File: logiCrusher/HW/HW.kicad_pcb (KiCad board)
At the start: 2 copper layers, 33 x 90 mm, 49 parts, among them J1 Left, J3 Conn_02x05_Odd_Even, J4 Right, U1 LM2904DR, U2 LM2904DR, U3 R-783.3-0.5, U4 STM32F373CCTx, U5 LM2904DR, U6 LM2904DR

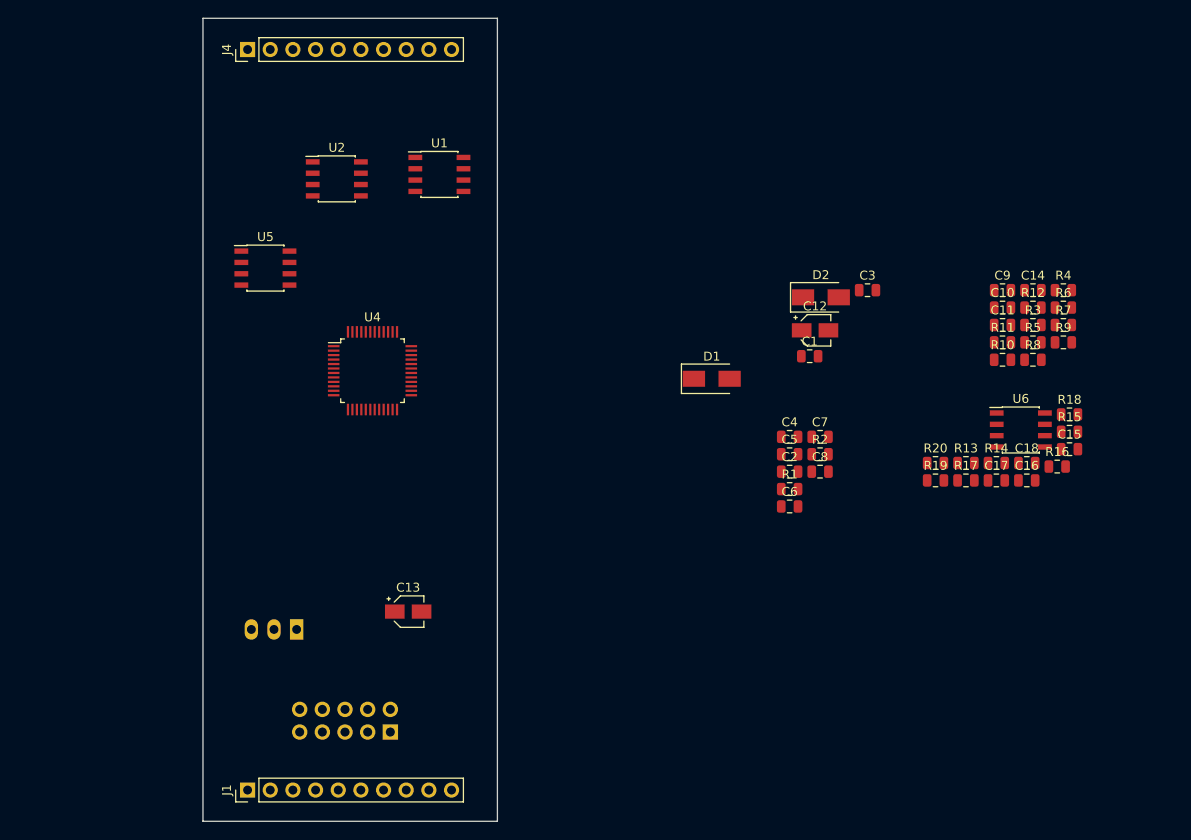
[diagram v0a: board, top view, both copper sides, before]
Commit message: Worked on the layout for the logicrusher
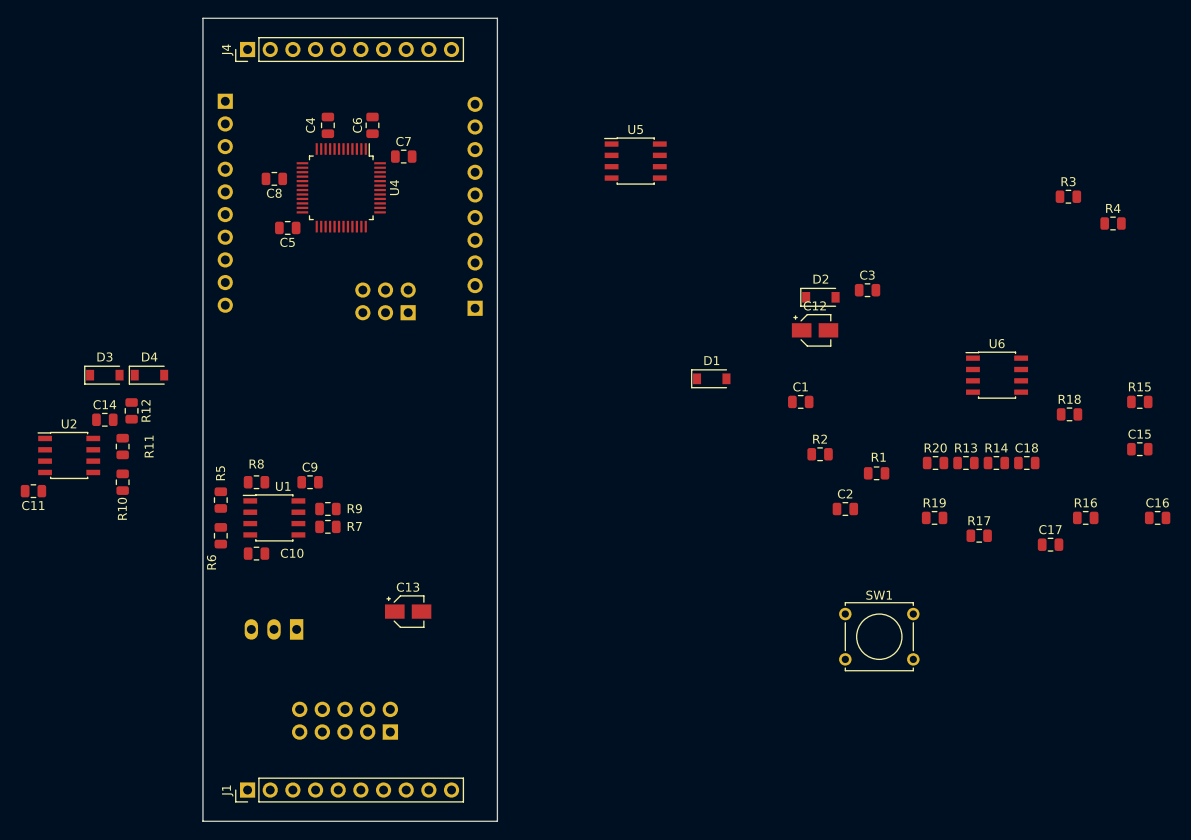
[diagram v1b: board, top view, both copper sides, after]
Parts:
- added D3: 1N5819HW-7-F, Diode_SMD:D_SOD-123, F.Cu at (99.0, 100.0)
- added D4: 1N5819HW-7-F, Diode_SMD:D_SOD-123, F.Cu at (104.0, 100.0)
- added J2: Conn_02x03_Odd_Even, Connector_PinHeader_2.54mm:PinHeader_2x03_P2.54mm_Vertical, B.Cu at (133.0, 93.0)
- added J5: Conn_01x10, Connector_PinHeader_2.54mm:PinHeader_1x10_P2.54mm_Vertical, B.Cu at (140.5, 92.5)
- added J6: Conn_01x10, Connector_PinHeader_2.54mm:PinHeader_1x10_P2.54mm_Vertical, B.Cu at (112.5, 69.3)
- added SW1: SW_Push, Button_Switch_THT:SW_Tactile_Straight_KSL0Axx1LFTR, F.Cu at (182.0, 126.8)
- D1, D2: value STTH102A -> 1N5819HW-7-F; footprint Diode_SMD:D_SMA -> Diode_SMD:D_SOD-123
- moved C11 110.2 mm to (91.0, 113.0), turned to 180 degrees
- moved C14 105.0 mm to (99.0, 105.0)
- moved R12 101.7 mm to (102.0, 104.0), turned to 270 degrees
- moved R10 99.6 mm to (101.0, 112.0), turned to 270 degrees
- moved R11 99.3 mm to (101.0, 108.0), turned to 270 degrees
- moved R6 97.8 mm to (112.0, 118.0), turned to 90 degrees
- moved R5 92.7 mm to (112.0, 114.0), turned to 270 degrees
- moved R8 88.1 mm to (116.0, 112.0), turned to 180 degrees
- moved C10 88.0 mm to (116.0, 120.0)
- moved R7 85.5 mm to (124.0, 117.0)
- moved R9 84.5 mm to (124.0, 115.0)
- moved C9 80.5 mm to (122.0, 112.0)
- moved C8 69.4 mm to (118.0, 78.0), turned to 180 degrees
- moved C6 63.3 mm to (129.0, 72.0), turned to 90 degrees
- moved C4 62.4 mm to (124.0, 72.0), turned to 90 degrees
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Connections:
- R20 pad 2: /OUT_Cond/Vout -> /AOUT0
- R5 pad 1: /IN_Cond/Vin -> /AIN0
- U4 pad 10: /MCU/ADC0 -> /POT3
- U4 pad 11: /MCU/ADC1 -> /POT2
- U4 pad 12: /MCU/ADC2 -> /POT1
- U4 pad 13: /MCU/ADC3 -> /POT0
- U4 pad 14: /MCU/Vout -> /OUT_Cond/Vin

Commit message: Spend a lot of time working on the logicCrusher HW
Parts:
- SW1: moved to B.Cu
- moved R4 102.7 mm to (111.5, 104.0), turned to 270 degrees
- moved R3 97.6 mm to (111.5, 100.2), turned to 270 degrees
- moved C16 86.9 mm to (130.5, 107.2), turned to 90 degrees
- moved C17 78.8 mm to (126.2, 122.5), turned to 90 degrees
- moved R15 78.6 mm to (136.5, 106.2), turned to 180 degrees
- moved C3 77.2 mm to (116.0, 126.0)
- moved C15 76.8 mm to (138.5, 115.2), turned to 270 degrees
- moved R16 74.4 mm to (134.5, 116.2)
- moved U6 73.7 mm to (130.2, 126.5), turned to 270 degrees
- moved R18 71.7 mm to (137.0, 119.2), turned to 270 degrees
- moved C18 71.0 mm to (134.2, 130.0), turned to 270 degrees
- moved R14 68.2 mm to (131.0, 116.2)
- moved R20 66.2 mm to (129.8, 132.0), turned to 270 degrees
- moved D2 64.3 mm to (133.5, 136.5), turned to 90 degrees
- moved R17 62.0 mm to (136.5, 104.2), turned to 180 degrees
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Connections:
- J1 pad 7: /DOUT0 -> /D0
- J1 pad 8: /DOUT1 -> /D1
- J1 pad 9: /DOUT2 -> /D2
- J4 pad 7: /DIN0 -> /D3
- J4 pad 8: /DIN1 -> /D4
- J4 pad 9: /DIN2 -> /D5
- J5 pad 1: Net-(J5-Pad1) -> /D0
- J5 pad 2: Net-(J5-Pad2) -> /D1
- J5 pad 3: Net-(J5-Pad3) -> /D2
- J5 pad 4: Net-(J5-Pad4) -> /D3
- J5 pad 5: Net-(J5-Pad5) -> /D4
- J5 pad 6: Net-(J5-Pad6) -> /D5
- U4 pad 18: Net-(J5-Pad1) -> /D0
- U4 pad 19: Net-(J5-Pad2) -> /D1
- U4 pad 39: Net-(J5-Pad3) -> /D2
- U4 pad 40: Net-(J5-Pad4) -> /D3
- U4 pad 41: Net-(J5-Pad5) -> /D4
- U4 pad 42: Net-(J5-Pad6) -> /D5
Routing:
- net +3V3: track 0.00 -> 130.1 mm, vias 0 -> 5
- net /D1: track 0.00 -> 89.8 mm, vias 0 -> 1
- net /D0: track 0.00 -> 89.0 mm, vias 0 -> 2
- net +12V: track 0.00 -> 85.4 mm, vias 0 -> 1
- net -12V: track 0.00 -> 79.3 mm, vias 0 -> 3
- net /D2: track 0.00 -> 79.1 mm, vias 0 -> 1
- net /OUT_Cond/Vin: track 0.00 -> 63.9 mm, vias 0 -> 3
- net +1.65V: track 0.00 -> 42.8 mm, vias 0 -> 3
- net /MCU/nRST: track 0.00 -> 38.3 mm, vias 0 -> 1
- net /D3: track 0.00 -> 38.2 mm, vias 0 -> 1
- net /AIN0: track 0.00 -> 36.5 mm
- net /D4: track 0.00 -> 33.8 mm, vias 0 -> 1
- net /D5: track 0.00 -> 29.3 mm, vias 0 -> 1
- net Net-(J5-Pad10): track 0.00 -> 23.9 mm, vias 0 -> 1
- net /POT3: track 0.00 -> 23.1 mm, vias 0 -> 1
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- added copper zone on B.Cu, net GND
- added copper zone on F.Cu, net GND
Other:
- net class Default: clearance 0.2 -> 0.127; trace_width 0.25 -> 0.127
- net class Power added: clearance 0.2, trace_width 1, via_dia 0.8, via_drill 0.4
- rule trace_clearance: 0.2 -> 0.127
- rule trace_min: 0.2 -> 0.127

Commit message: Made fabrication files
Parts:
- J1, J4: footprint Connector_PinHeader_2.54mm:PinHeader_1x10_P2.54mm_Vertical -> Connector_PinSocket_2.54mm:PinSocket_1x10_P2.54mm_Vertical
- SW1: value SW_Push -> TL1105SPF250Q; footprint Button_Switch_THT:SW_Tactile_Straight_KSL0Axx1LFTR -> Eurocad:TL1105SPF250Q
- moved SW1 4.61 mm to (137.5, 100.0)
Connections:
- SW1 pad 1: GND -> /MCU/nRST
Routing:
- net /MCU/nRST: track 38.3 -> 39.8 mm
- net GND: vias 36 -> 35
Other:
- board text added: "KEY"

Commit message: pushing those gerbs I was refering to in the last commit
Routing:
- net /D0: track 89.0 -> 89.7 mm
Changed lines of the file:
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@@
     (thickness 1.6)
     (drawings 7)
-    (tracks 511)
+    (tracks 512)
     (zones 0)
     (modules 55)
@@
     (last_trace_width 0.127)
     (trace_clearance 0.127)
-    (zone_clearance 0.508)
+    (zone_clearance 0.127)
     (zone_45_only no)
     (trace_min 0.127)
@@
   (segment (start 138.25 92.5) (end 140.5 92.5) (width 0.127) (layer B.Cu) (net 64))
   (segment (start 124.75 79) (end 138.25 92.5) (width 0.127) (layer B.Cu) (net 64))
-  (segment (start 131.089999 145.650001) (end 131.849999 145.650001) (width 0.127) (layer B.Cu) (net 64))
-  (segment (start 130.24 146.5) (end 131.089999 145.650001) (width 0.127) (layer B.Cu) (net 64))
-  (segment (start 131.849999 145.650001) (end 135.25 142.25) (width 0.127) (layer B.Cu) (net 64))
-  (segment (start 135.25 142.25) (end 140.5 142.25) (width 0.127) (layer B.Cu) (net 64))
-  (segment (start 140.5 142.25) (end 141.5 141.25) (width 0.127) (layer B.Cu) (net 64))
-  (segment (start 141.5 141.25) (end 141.5 119.75) (width 0.127) (layer B.Cu) (net 64))
-  (segment (start 141.5 119.75) (end 141.5 104.25) (width 0.127) (layer B.Cu) (net 64))
-  (segment (start 141.5 104.25) (end 139.5 102.25) (width 0.127) (layer B.Cu) (net 64))
-  (segment (start 139.5 102.25) (end 139.5 98.25) (width 0.127) (layer B.Cu) (net 64))
   (segment (start 139.5 98.25) (end 139.5 98.25) (width 0.127) (layer B.Cu) (net 64))
   (via (at 139.5 98.25) (size 0.8) (drill 0.4) (layers F.Cu B.Cu) (net 64))
@@
   (segment (start 139.5 92.523) (end 139.523 92.5) (width 0.127) (layer F.Cu) (net 64))
   (segment (start 139.5 98.25) (end 139.5 92.523) (width 0.127) (layer F.Cu) (net 64))
+  (segment (start 140.25 104.25) (end 139.5 103.5) (width 0.127) (layer B.Cu) (net 64))
+  (segment (start 141.5 104.25) (end 140.25 104.25) (width 0.127) (layer B.Cu) (net 64))
+  (segment (start 141.5 141.25) (end 141.5 104.25) (width 0.127) (layer B.Cu) (net 64))
+  (segment (start 140.5 142.25) (end 141.5 141.25) (width 0.127) (layer B.Cu) (net 64))
+  (segment (start 139.5 103.5) (end 139.5 102.25) (width 0.127) (layer B.Cu) (net 64))
+  (segment (start 130.24 146.5) (end 131.089999 145.650001) (width 0.127) (layer B.Cu) (net 64))
+  (segment (start 131.089999 145.650001) (end 131.849999 145.650001) (width 0.127) (layer B.Cu) (net 64))
+  (segment (start 131.849999 145.650001) (end 135.25 142.25) (width 0.127) (layer B.Cu) (net 64))
+  (segment (start 139.5 102.25) (end 139.5 98.25) (width 0.127) (layer B.Cu) (net 64))
+  (segment (start 135.25 142.25) (end 140.5 142.25) (width 0.127) (layer B.Cu) (net 64))
   (via (at 122.75 79.75) (size 0.5) (drill 0.3) (layers F.Cu B.Cu) (net 65))
   (segment (start 121.15 79.25) (end 121.927 79.25) (width 0.127) (layer F.Cu) (net 65))
@@
   (segment (start 135.32 63.5) (end 135.32 74.62) (width 0.127) (layer F.Cu) (net 69))
   (zone (net 2) (net_name GND) (layer B.Cu) (hatch edge 0.508)
-    (connect_pads (clearance 0.508))
+    (connect_pads (clearance 0.127))
     (min_thickness 0.254)
     (fill yes (arc_segments 16) (thermal_gap 0.508) (thermal_bridge_width 0.508))
@@
   )
   (zone (net 2) (net_name GND) (layer F.Cu) (hatch edge 0.508)
-    (connect_pads thru_hole_only (clearance 0.508))
+    (connect_pads thru_hole_only (clearance 0.127))
     (min_thickness 0.1)
     (fill yes (arc_segments 16) (thermal_gap 0.508) (thermal_bridge_width 0.508))
